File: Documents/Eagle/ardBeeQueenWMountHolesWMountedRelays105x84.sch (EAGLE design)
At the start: 12 parts

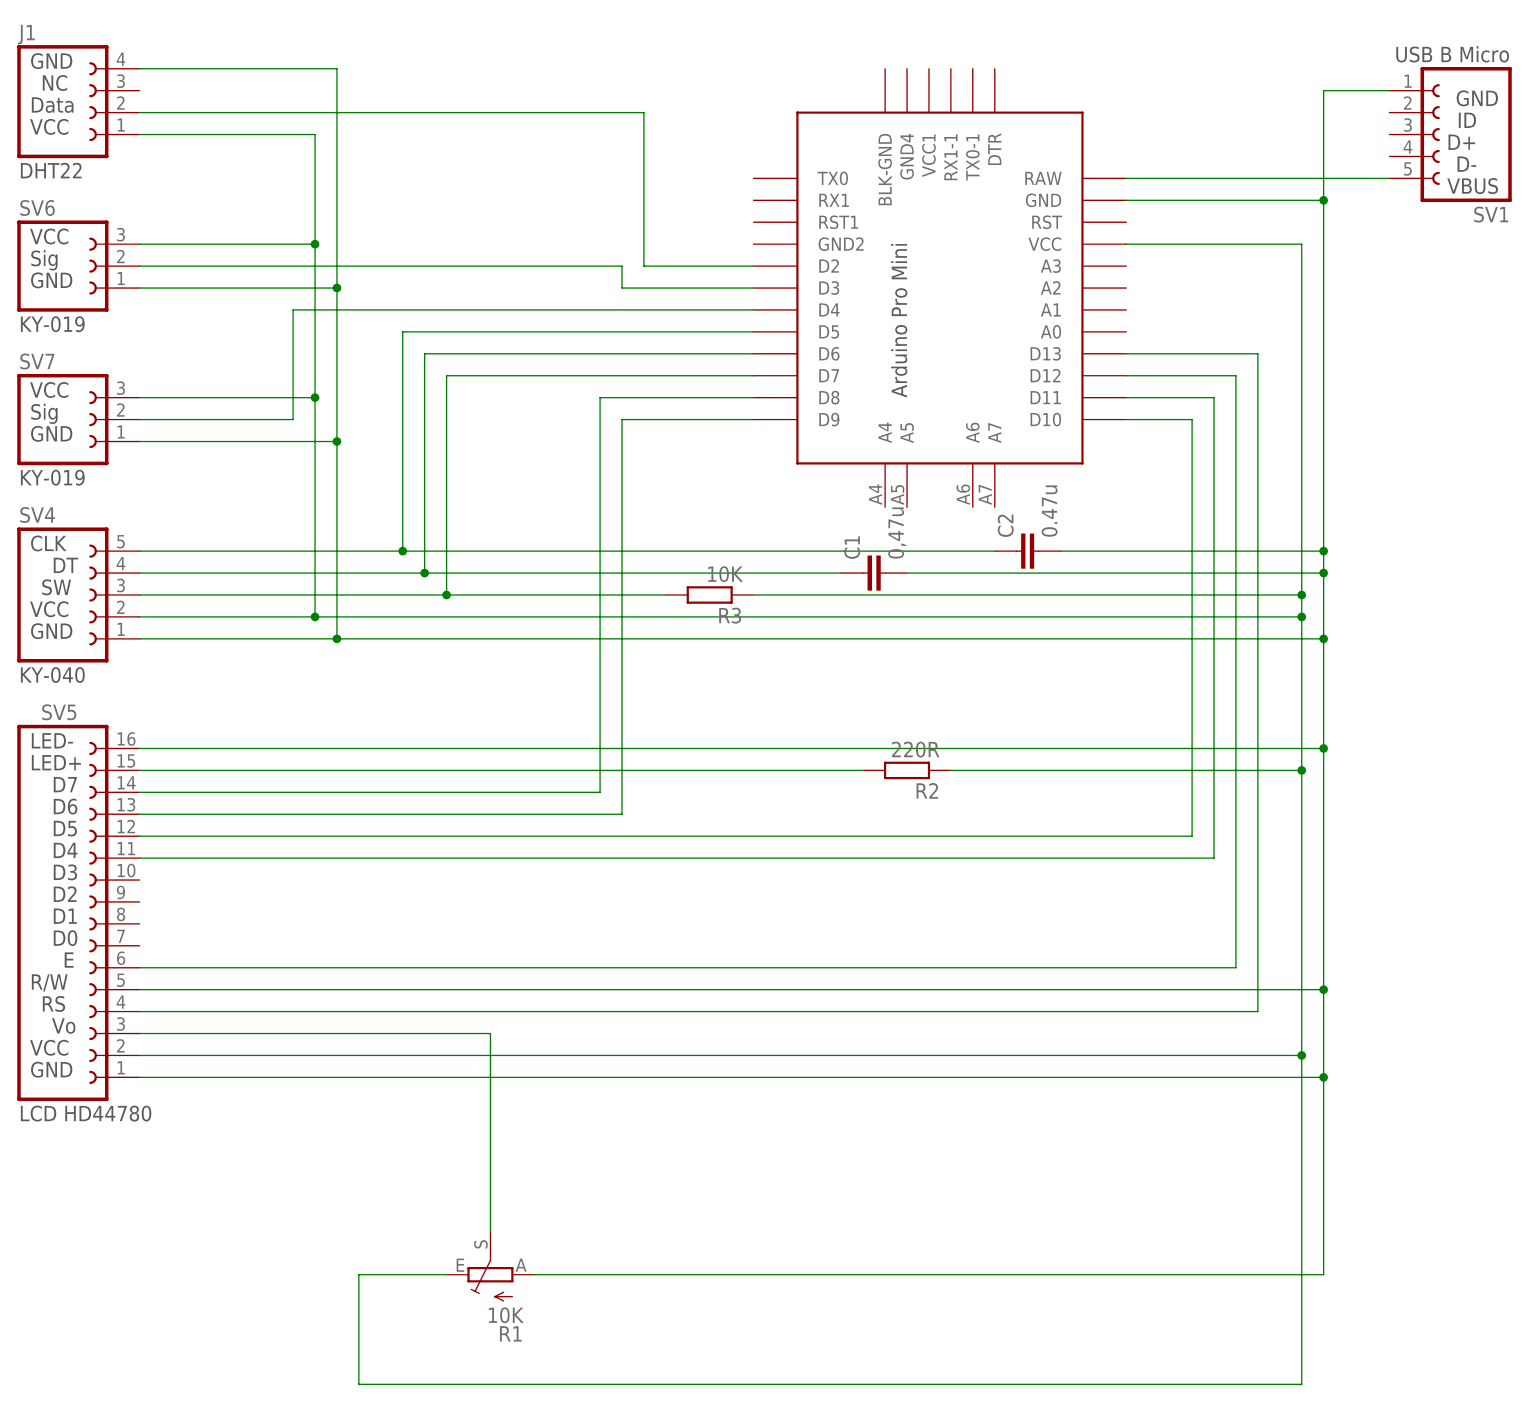
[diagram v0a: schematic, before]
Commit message: updated eagle docs
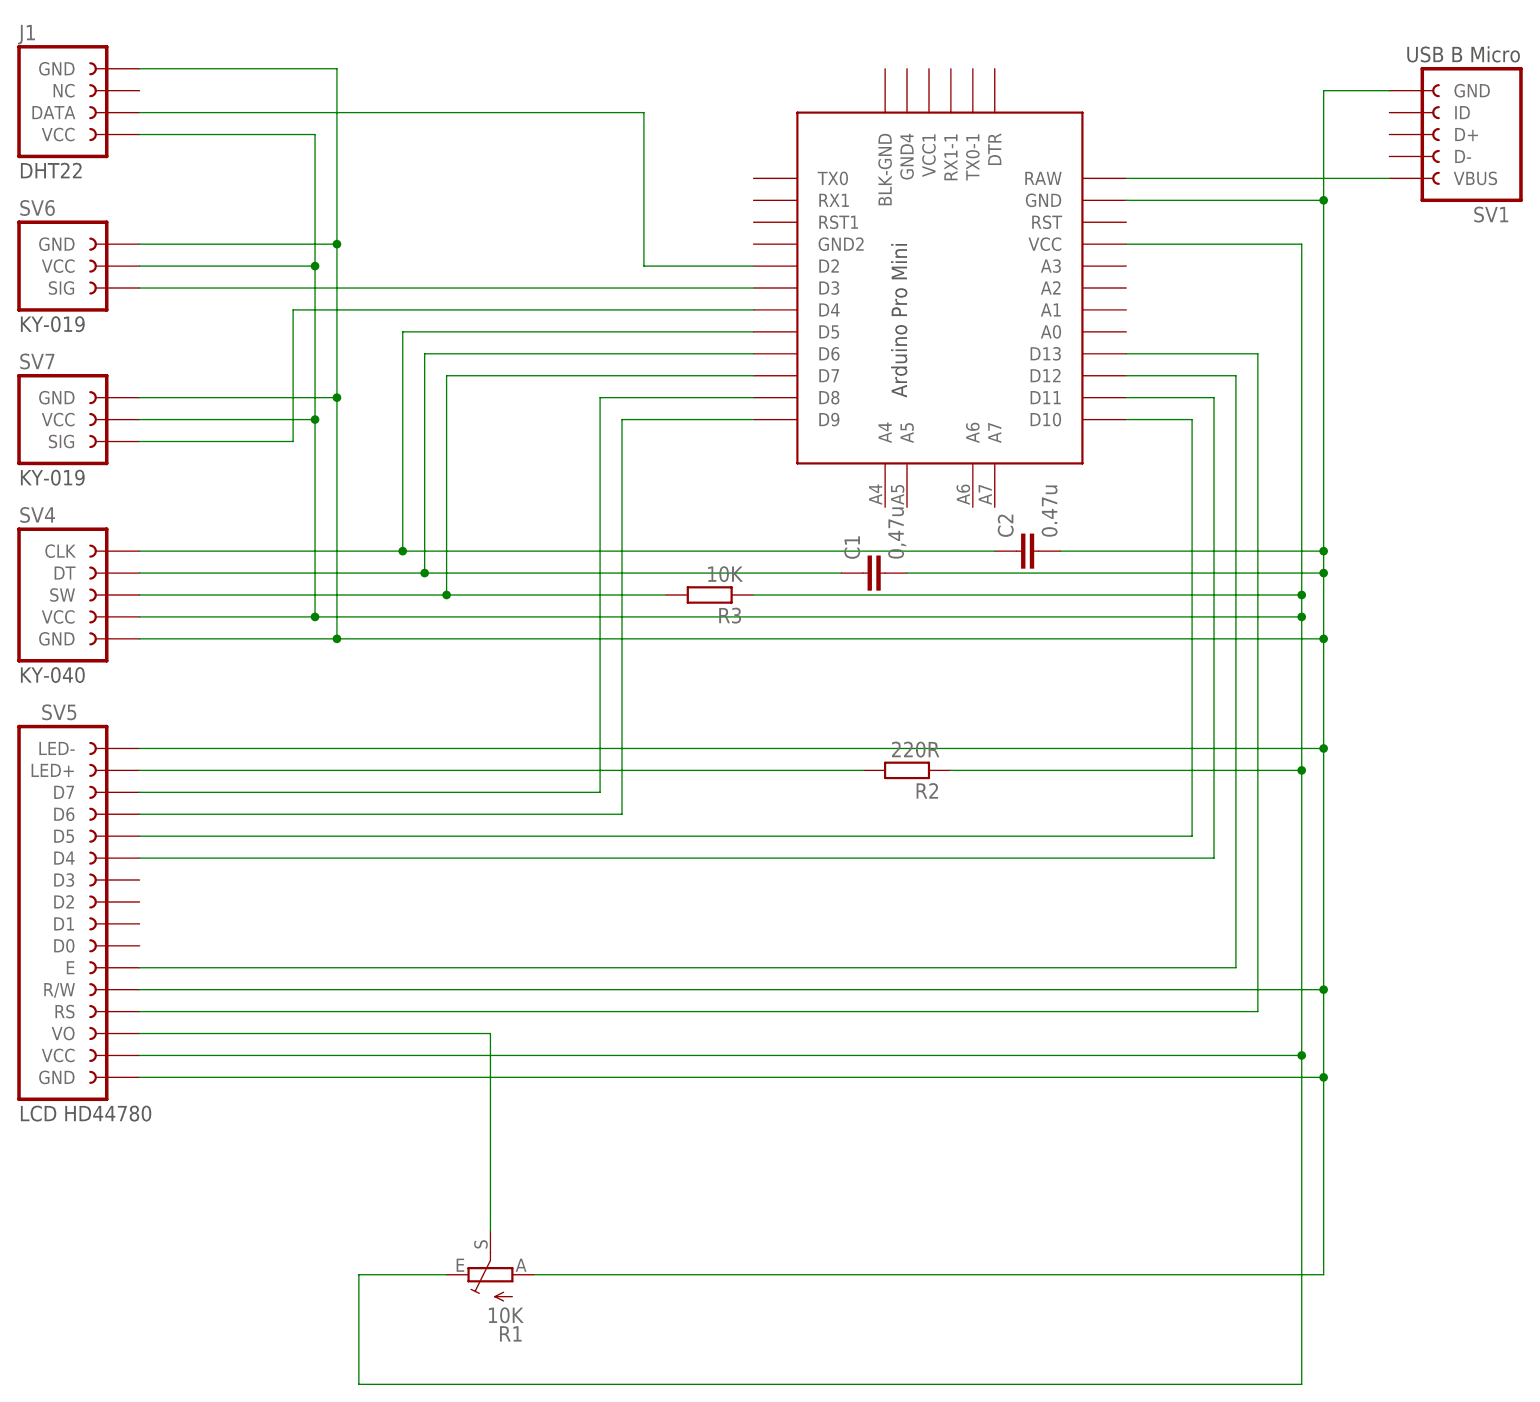
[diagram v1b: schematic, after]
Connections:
- net N$1: now also SV5.VO; no longer SV5.3
- net N$10: now also SV4.DT; no longer SV4.4
- net N$11: now also SV4.CLK; no longer SV4.5
- net N$12: now also J1.DATA; no longer J1.2
- net N$13: now also SV6.SIG; no longer SV6.2
- net N$14: now also SV7.SIG; no longer SV7.2
- net N$15: now also J1.VCC, SV4.VCC, SV5.VCC, SV6.VCC, SV7.VCC; no longer J1.1, SV4.2, SV5.2, SV6.3, SV7.3
- net N$16: now also J1.GND, SV1.GND, SV4.GND, SV5.GND, SV5.LED-, SV5.R/W, SV6.GND, SV7.GND; no longer J1.4, SV1.1, SV4.1, SV5.1, SV5.16, SV5.5, SV6.1, SV7.1
- net N$17: now also SV1.VBUS; no longer SV1.5
- net N$2: now also SV5.LED+; no longer SV5.15
- net N$3: now also SV5.D6; no longer SV5.13
- net N$4: now also SV5.D7; no longer SV5.14
- net N$5: now also SV5.D5; no longer SV5.12
- net N$6: now also SV5.D4; no longer SV5.11
- net N$7: now also SV5.E; no longer SV5.6
- net N$8: now also SV5.RS; no longer SV5.4
- net N$9: now also SV4.SW; no longer SV4.3
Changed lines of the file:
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@@
 <wire x1="152.4" y1="104.14" x2="193.04" y2="104.14" width="0.1524" layer="91"/>
 <wire x1="193.04" y1="104.14" x2="193.04" y2="81.28" width="0.1524" layer="91"/>
-<pinref part="SV5" gate="G$1" pin="3"/>
+<pinref part="SV5" gate="G$1" pin="VO"/>
 </segment>
 </net>
@@
 <pinref part="R2" gate="G$1" pin="2"/>
 <wire x1="236.22" y1="134.62" x2="152.4" y2="134.62" width="0.1524" layer="91"/>
-<pinref part="SV5" gate="G$1" pin="15"/>
+<pinref part="SV5" gate="G$1" pin="LED+"/>
 </segment>
 </net>
@@
 <wire x1="274.32" y1="175.26" x2="266.7" y2="175.26" width="0.1524" layer="91"/>
 <pinref part="U$1" gate="G$1" pin="D10"/>
-<pinref part="SV5" gate="G$1" pin="12"/>
+<pinref part="SV5" gate="G$1" pin="D5"/>
 </segment>
 </net>
@@
 <wire x1="276.86" y1="177.8" x2="266.7" y2="177.8" width="0.1524" layer="91"/>
 <pinref part="U$1" gate="G$1" pin="D11"/>
-<pinref part="SV5" gate="G$1" pin="11"/>
+<pinref part="SV5" gate="G$1" pin="D4"/>
 </segment>
 </net>
@@
 <wire x1="279.4" y1="180.34" x2="266.7" y2="180.34" width="0.1524" layer="91"/>
 <pinref part="U$1" gate="G$1" pin="D12"/>
-<pinref part="SV5" gate="G$1" pin="6"/>
+<pinref part="SV5" gate="G$1" pin="E"/>
 </segment>
 </net>
@@
 <wire x1="281.94" y1="182.88" x2="266.7" y2="182.88" width="0.1524" layer="91"/>
 <pinref part="U$1" gate="G$1" pin="D13"/>
-<pinref part="SV5" gate="G$1" pin="4"/>
+<pinref part="SV5" gate="G$1" pin="RS"/>
 </segment>
 </net>
@@
 <junction x="187.96" y="154.94"/>
 <pinref part="U$1" gate="G$1" pin="D7"/>
-<pinref part="SV4" gate="G$1" pin="3"/>
+<pinref part="SV4" gate="G$1" pin="SW"/>
 </segment>
 </net>
@@
 <junction x="185.42" y="157.48"/>
 <pinref part="U$1" gate="G$1" pin="D6"/>
-<pinref part="SV4" gate="G$1" pin="4"/>
+<pinref part="SV4" gate="G$1" pin="DT"/>
 </segment>
 </net>
@@
 <junction x="182.88" y="160.02"/>
 <pinref part="U$1" gate="G$1" pin="D5"/>
-<pinref part="SV4" gate="G$1" pin="5"/>
+<pinref part="SV4" gate="G$1" pin="CLK"/>
 </segment>
 </net>
@@
 <wire x1="210.82" y1="193.04" x2="223.52" y2="193.04" width="0.1524" layer="91"/>
 <pinref part="U$1" gate="G$1" pin="D2"/>
-<pinref part="J1" gate="G$1" pin="2"/>
+<pinref part="J1" gate="G$1" pin="DATA"/>
 </segment>
 </net>
 <net name="N$13" class="0">
 <segment>
-<wire x1="152.4" y1="193.04" x2="208.28" y2="193.04" width="0.1524" layer="91"/>
-<wire x1="208.28" y1="193.04" x2="208.28" y2="190.5" width="0.1524" layer="91"/>
-<wire x1="208.28" y1="190.5" x2="223.52" y2="190.5" width="0.1524" layer="91"/>
 <pinref part="U$1" gate="G$1" pin="D3"/>
-<pinref part="SV6" gate="G$1" pin="2"/>
+<pinref part="SV6" gate="G$1" pin="SIG"/>
+<wire x1="152.4" y1="190.5" x2="223.52" y2="190.5" width="0.1524" layer="91"/>
 </segment>
 </net>
 <net name="N$14" class="0">
 <segment>
-<wire x1="152.4" y1="175.26" x2="170.18" y2="175.26" width="0.1524" layer="91"/>
-<wire x1="170.18" y1="175.26" x2="170.18" y2="187.96" width="0.1524" layer="91"/>
+<wire x1="170.18" y1="172.72" x2="170.18" y2="187.96" width="0.1524" layer="91"/>
 <wire x1="170.18" y1="187.96" x2="223.52" y2="187.96" width="0.1524" layer="91"/>
 <pinref part="U$1" gate="G$1" pin="D4"/>
-<pinref part="SV7" gate="G$1" pin="2"/>
+<pinref part="SV7" gate="G$1" pin="SIG"/>
+<wire x1="170.18" y1="172.72" x2="152.4" y2="172.72" width="0.1524" layer="91"/>
 </segment>
 </net>
@@
 <wire x1="208.28" y1="175.26" x2="223.52" y2="175.26" width="0.1524" layer="91"/>
 <pinref part="U$1" gate="G$1" pin="D9"/>
-<pinref part="SV5" gate="G$1" pin="13"/>
+<pinref part="SV5" gate="G$1" pin="D6"/>
 </segment>
 </net>
@@
 <wire x1="205.74" y1="177.8" x2="223.52" y2="177.8" width="0.1524" layer="91"/>
 <pinref part="U$1" gate="G$1" pin="D8"/>
-<pinref part="SV5" gate="G$1" pin="14"/>
+<pinref part="SV5" gate="G$1" pin="D7"/>
 </segment>
 </net>
@@
 <wire x1="172.72" y1="152.4" x2="287.02" y2="152.4" width="0.1524" layer="91"/>
 <wire x1="223.52" y1="154.94" x2="287.02" y2="154.94" width="0.1524" layer="91"/>
-<wire x1="172.72" y1="152.4" x2="172.72" y2="177.8" width="0.1524" layer="91"/>
-<wire x1="172.72" y1="177.8" x2="172.72" y2="195.58" width="0.1524" layer="91"/>
-<wire x1="172.72" y1="195.58" x2="172.72" y2="208.28" width="0.1524" layer="91"/>
+<wire x1="172.72" y1="152.4" x2="172.72" y2="175.26" width="0.1524" layer="91"/>
+<wire x1="172.72" y1="175.26" x2="172.72" y2="193.04" width="0.1524" layer="91"/>
+<wire x1="172.72" y1="193.04" x2="172.72" y2="208.28" width="0.1524" layer="91"/>
 <wire x1="172.72" y1="208.28" x2="152.4" y2="208.28" width="0.1524" layer="91"/>
 <junction x="172.72" y="152.4"/>
-<wire x1="152.4" y1="195.58" x2="172.72" y2="195.58" width="0.1524" layer="91"/>
-<junction x="172.72" y="195.58"/>
-<wire x1="152.4" y1="177.8" x2="172.72" y2="177.8" width="0.1524" layer="91"/>
-<junction x="172.72" y="177.8"/>
 <wire x1="287.02" y1="154.94" x2="287.02" y2="195.58" width="0.1524" layer="91"/>
 <wire x1="287.02" y1="195.58" x2="266.7" y2="195.58" width="0.1524" layer="91"/>
 <junction x="287.02" y="154.94"/>
 <pinref part="U$1" gate="G$1" pin="VCC"/>
-<pinref part="J1" gate="G$1" pin="1"/>
-<pinref part="SV4" gate="G$1" pin="2"/>
-<pinref part="SV5" gate="G$1" pin="2"/>
-<pinref part="SV6" gate="G$1" pin="3"/>
-<pinref part="SV7" gate="G$1" pin="3"/>
+<pinref part="J1" gate="G$1" pin="VCC"/>
+<pinref part="SV4" gate="G$1" pin="VCC"/>
+<pinref part="SV5" gate="G$1" pin="VCC"/>
+<pinref part="SV6" gate="G$1" pin="VCC"/>
+<wire x1="152.4" y1="193.04" x2="172.72" y2="193.04" width="0.1524" layer="91"/>
+<junction x="172.72" y="193.04"/>
+<pinref part="SV7" gate="G$1" pin="VCC"/>
+<wire x1="152.4" y1="175.26" x2="172.72" y2="175.26" width="0.1524" layer="91"/>
+<junction x="172.72" y="175.26"/>
 </segment>
 </net>
@@
 <wire x1="259.08" y1="160.02" x2="289.56" y2="160.02" width="0.1524" layer="91"/>
 <junction x="289.56" y="160.02"/>
-<wire x1="175.26" y1="149.86" x2="175.26" y2="172.72" width="0.1524" layer="91"/>
-<wire x1="175.26" y1="172.72" x2="175.26" y2="190.5" width="0.1524" layer="91"/>
-<wire x1="175.26" y1="190.5" x2="175.26" y2="215.9" width="0.1524" layer="91"/>
+<wire x1="175.26" y1="149.86" x2="175.26" y2="177.8" width="0.1524" layer="91"/>
+<wire x1="175.26" y1="177.8" x2="175.26" y2="195.58" width="0.1524" layer="91"/>
+<wire x1="175.26" y1="195.58" x2="175.26" y2="215.9" width="0.1524" layer="91"/>
 <wire x1="175.26" y1="215.9" x2="152.4" y2="215.9" width="0.1524" layer="91"/>
 <junction x="175.26" y="149.86"/>
-<wire x1="152.4" y1="190.5" x2="175.26" y2="190.5" width="0.1524" layer="91"/>
-<junction x="175.26" y="190.5"/>
-<wire x1="152.4" y1="172.72" x2="175.26" y2="172.72" width="0.1524" layer="91"/>
-<junction x="175.26" y="172.72"/>
 <wire x1="289.56" y1="200.66" x2="289.56" y2="213.36" width="0.1524" layer="91"/>
 <junction x="289.56" y="200.66"/>
-<pinref part="SV1" gate="G$1" pin="1"/>
+<pinref part="SV1" gate="G$1" pin="GND"/>
 <wire x1="289.56" y1="213.36" x2="297.18" y2="213.36" width="0.1524" layer="91"/>
 <pinref part="U$1" gate="G$1" pin="GND"/>
-<pinref part="J1" gate="G$1" pin="4"/>
-<pinref part="SV4" gate="G$1" pin="1"/>
-<pinref part="SV5" gate="G$1" pin="1"/>
-<pinref part="SV5" gate="G$1" pin="5"/>
-<pinref part="SV5" gate="G$1" pin="16"/>
-<pinref part="SV6" gate="G$1" pin="1"/>
-<pinref part="SV7" gate="G$1" pin="1"/>
+<pinref part="J1" gate="G$1" pin="GND"/>
+<pinref part="SV4" gate="G$1" pin="GND"/>
+<pinref part="SV5" gate="G$1" pin="GND"/>
+<pinref part="SV5" gate="G$1" pin="R/W"/>
+<pinref part="SV5" gate="G$1" pin="LED-"/>
+<pinref part="SV6" gate="G$1" pin="GND"/>
+<wire x1="152.4" y1="195.58" x2="175.26" y2="195.58" width="0.1524" layer="91"/>
+<junction x="175.26" y="195.58"/>
+<pinref part="SV7" gate="G$1" pin="GND"/>
+<wire x1="152.4" y1="177.8" x2="175.26" y2="177.8" width="0.1524" layer="91"/>
+<junction x="175.26" y="177.8"/>
 </segment>
 </net>
@@
 <segment>
 <wire x1="266.7" y1="203.2" x2="297.18" y2="203.2" width="0.1524" layer="91"/>
-<pinref part="SV1" gate="G$1" pin="5"/>
+<pinref part="SV1" gate="G$1" pin="VBUS"/>
 <pinref part="U$1" gate="G$1" pin="RAW"/>
 </segment>
